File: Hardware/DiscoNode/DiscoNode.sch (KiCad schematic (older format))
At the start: 68 parts, among them J1 1267, J2 RJ45, J3 RJ45, J4 AVR-ISP-6, J5 Debug, J6 0026605020, Q1 NTR4003N, Q2 NTR4003N, Q3 NTR4003N, U1 ATMEGA328P-AU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

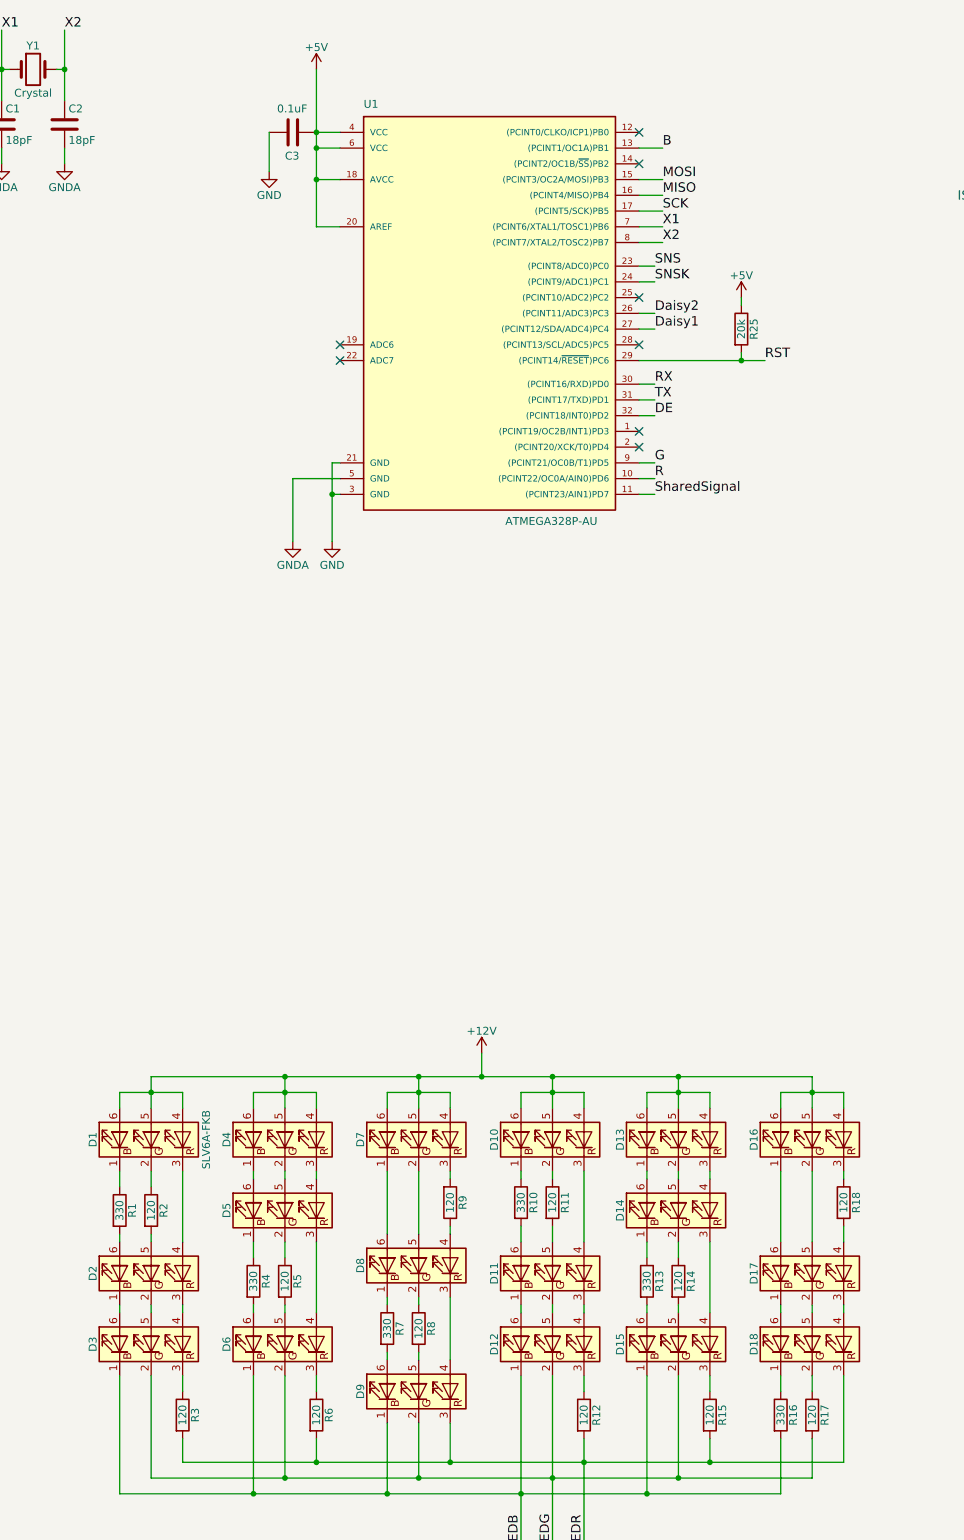
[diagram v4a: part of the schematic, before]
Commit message: Move debug pins.
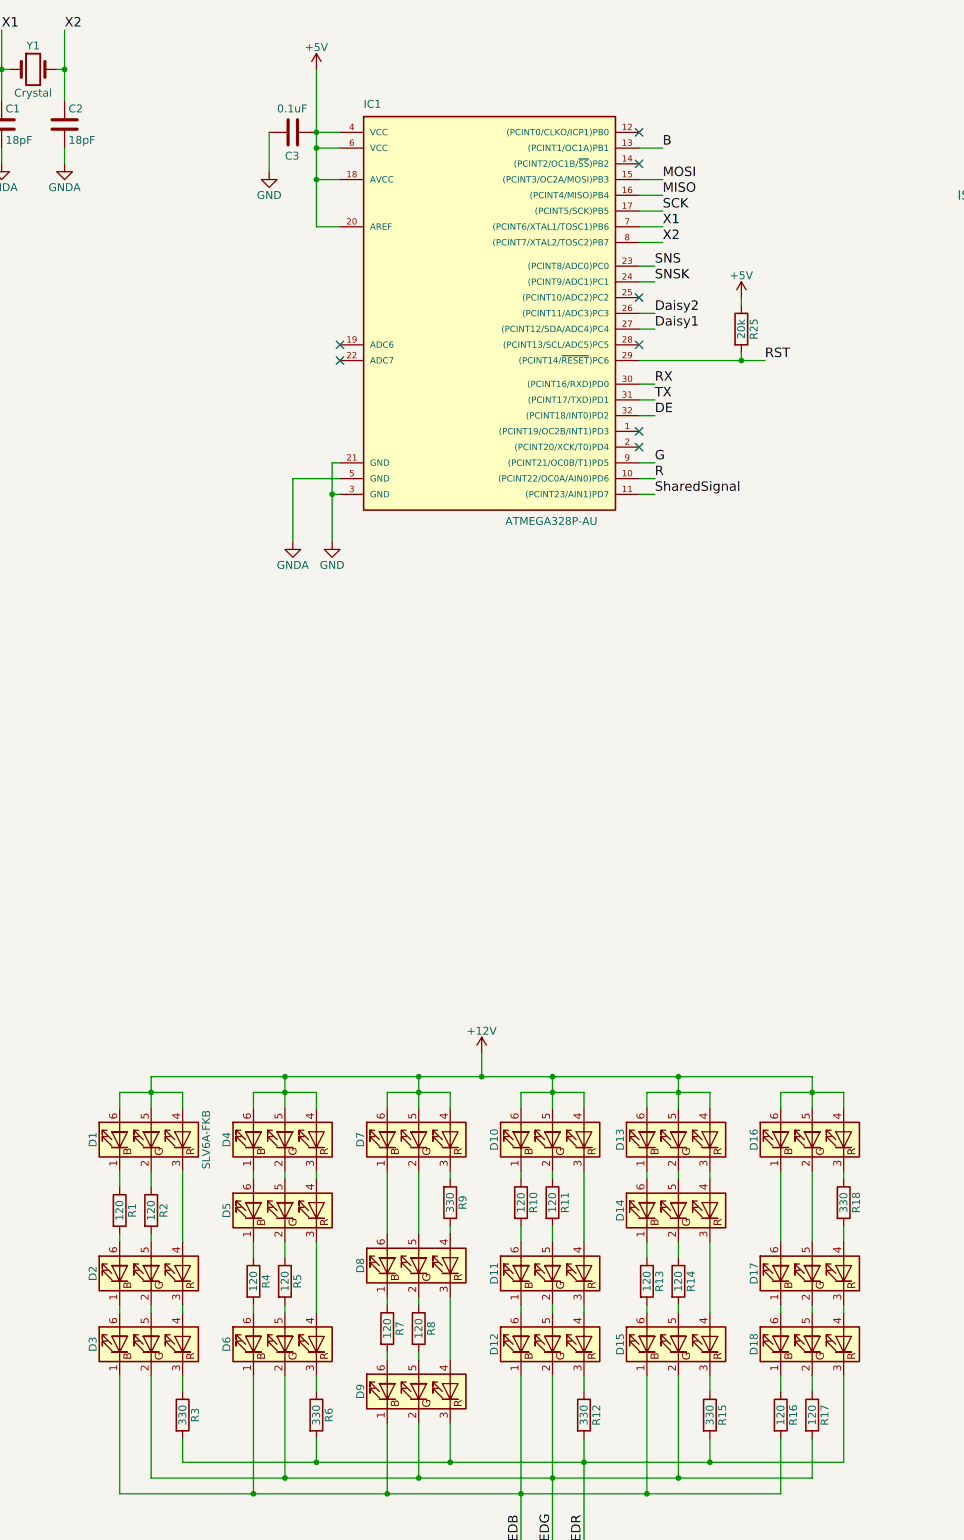
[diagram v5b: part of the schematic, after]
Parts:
- R1, R10, R13, R16, R4, R7: value 330 -> 120; Digikey RMCF0805JT330RCT-ND -> (none); MPN RMCF0805JT330R -> RMCF0805JT120R
- R12, R15, R18, R3, R6, R9: value 120 -> 330; Digikey RMCF0805JT120RCT-ND -> (none); MPN RMCF0805JT120R -> RMCF0805JT330R
- R2: Digikey RMCF0805JT120RCT-ND -> (none)
- renumbered U1 to IC1
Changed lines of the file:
@@
 P 1750 8450
 F 0 "R1" V 1830 8450 50  0000 C CNN
-F 1 "330" V 1750 8450 50  0000 C CNN
+F 1 "120" V 1750 8450 50  0000 C CNN
 F 2 "Resistors_SMD:R_0805" V 1680 8450 50  0001 C CNN
 F 3 "" H 1750 8450 50  0000 C CNN
-F 4 "RMCF0805JT330R" H 1750 8450 60  0001 C CNN "MPN"
-F 5 "RMCF0805JT330RCT-ND" H 1750 8450 60  0001 C CNN "Digikey"
+F 4 "RMCF0805JT120R" H 1750 8450 60  0001 C CNN "MPN"
 	1    1750 8450
 	1    0    0    -1
@@
 F 3 "" H 1950 8450 50  0000 C CNN
 F 4 "RMCF0805JT120R" H 1950 8450 60  0001 C CNN "MPN"
-F 5 "RMCF0805JT120RCT-ND" H 1950 8450 60  0001 C CNN "Digikey"
 	1    1950 8450
 	1    0    0    -1
@@
 P 2150 9750
 F 0 "R3" V 2230 9750 50  0000 C CNN
-F 1 "120" V 2150 9750 50  0000 C CNN
+F 1 "330" V 2150 9750 50  0000 C CNN
 F 2 "Resistors_SMD:R_0805" V 2080 9750 50  0001 C CNN
 F 3 "" H 2150 9750 50  0000 C CNN
-F 4 "RMCF0805JT120R" H 2150 9750 60  0001 C CNN "MPN"
-F 5 "RMCF0805JT120RCT-ND" H 2150 9750 60  0001 C CNN "Digikey"
+F 4 "RMCF0805JT330R" H 2150 9750 60  0001 C CNN "MPN"
 	1    2150 9750
 	1    0    0    -1
@@
 P 2600 8900
 F 0 "R4" V 2680 8900 50  0000 C CNN
-F 1 "330" V 2600 8900 50  0000 C CNN
+F 1 "120" V 2600 8900 50  0000 C CNN
 F 2 "Resistors_SMD:R_0805" V 2530 8900 50  0001 C CNN
 F 3 "" H 2600 8900 50  0000 C CNN
-F 4 "RMCF0805JT330R" H 2600 8900 60  0001 C CNN "MPN"
-F 5 "RMCF0805JT330RCT-ND" H 2600 8900 60  0001 C CNN "Digikey"
+F 4 "RMCF0805JT120R" H 2600 8900 60  0001 C CNN "MPN"
 	1    2600 8900
 	1    0    0    -1
@@
 P 3000 9750
 F 0 "R6" V 3080 9750 50  0000 C CNN
-F 1 "120" V 3000 9750 50  0000 C CNN
+F 1 "330" V 3000 9750 50  0000 C CNN
 F 2 "Resistors_SMD:R_0805" V 2930 9750 50  0001 C CNN
 F 3 "" H 3000 9750 50  0000 C CNN
-F 4 "RMCF0805JT120R" H 3000 9750 60  0001 C CNN "MPN"
-F 5 "RMCF0805JT120RCT-ND" H 3000 9750 60  0001 C CNN "Digikey"
+F 4 "RMCF0805JT330R" H 3000 9750 60  0001 C CNN "MPN"
 	1    3000 9750
 	1    0    0    -1
@@
 P 3450 9200
 F 0 "R7" V 3530 9200 50  0000 C CNN
-F 1 "330" V 3450 9200 50  0000 C CNN
+F 1 "120" V 3450 9200 50  0000 C CNN
 F 2 "Resistors_SMD:R_0805" V 3380 9200 50  0001 C CNN
 F 3 "" H 3450 9200 50  0000 C CNN
-F 4 "RMCF0805JT330R" H 3450 9200 60  0001 C CNN "MPN"
-F 5 "RMCF0805JT330RCT-ND" H 3450 9200 60  0001 C CNN "Digikey"
+F 4 "RMCF0805JT120R" H 3450 9200 60  0001 C CNN "MPN"
 	1    3450 9200
 	1    0    0    -1
@@
 P 3850 8400
 F 0 "R9" V 3930 8400 50  0000 C CNN
-F 1 "120" V 3850 8400 50  0000 C CNN
+F 1 "330" V 3850 8400 50  0000 C CNN
 F 2 "Resistors_SMD:R_0805" V 3780 8400 50  0001 C CNN
 F 3 "" H 3850 8400 50  0000 C CNN
-F 4 "RMCF0805JT120R" H 3850 8400 60  0001 C CNN "MPN"
-F 5 "RMCF0805JT120RCT-ND" H 3850 8400 60  0001 C CNN "Digikey"
+F 4 "RMCF0805JT330R" H 3850 8400 60  0001 C CNN "MPN"
 	1    3850 8400
 	1    0    0    1
@@
 P 4300 8400
 F 0 "R10" V 4380 8400 50  0000 C CNN
-F 1 "330" V 4300 8400 50  0000 C CNN
+F 1 "120" V 4300 8400 50  0000 C CNN
 F 2 "Resistors_SMD:R_0805" V 4230 8400 50  0001 C CNN
 F 3 "" H 4300 8400 50  0000 C CNN
-F 4 "RMCF0805JT330R" H 4300 8400 60  0001 C CNN "MPN"
-F 5 "RMCF0805JT330RCT-ND" H 4300 8400 60  0001 C CNN "Digikey"
+F 4 "RMCF0805JT120R" H 4300 8400 60  0001 C CNN "MPN"
 	1    4300 8400
 	1    0    0    -1
@@
 P 4700 9750
 F 0 "R12" V 4780 9750 50  0000 C CNN
-F 1 "120" V 4700 9750 50  0000 C CNN
+F 1 "330" V 4700 9750 50  0000 C CNN
 F 2 "Resistors_SMD:R_0805" V 4630 9750 50  0001 C CNN
 F 3 "" H 4700 9750 50  0000 C CNN
-F 4 "RMCF0805JT120R" H 4700 9750 60  0001 C CNN "MPN"
-F 5 "RMCF0805JT120RCT-ND" H 4700 9750 60  0001 C CNN "Digikey"
+F 4 "RMCF0805JT330R" H 4700 9750 60  0001 C CNN "MPN"
 	1    4700 9750
 	1    0    0    -1
@@
 P 5100 8900
 F 0 "R13" V 5180 8900 50  0000 C CNN
-F 1 "330" V 5100 8900 50  0000 C CNN
+F 1 "120" V 5100 8900 50  0000 C CNN
 F 2 "Resistors_SMD:R_0805" V 5030 8900 50  0001 C CNN
 F 3 "" H 5100 8900 50  0000 C CNN
-F 4 "RMCF0805JT330R" H 5100 8900 60  0001 C CNN "MPN"
-F 5 "RMCF0805JT330RCT-ND" H 5100 8900 60  0001 C CNN "Digikey"
+F 4 "RMCF0805JT120R" H 5100 8900 60  0001 C CNN "MPN"
 	1    5100 8900
 	1    0    0    -1
@@
 P 5500 9750
 F 0 "R15" V 5580 9750 50  0000 C CNN
-F 1 "120" V 5500 9750 50  0000 C CNN
+F 1 "330" V 5500 9750 50  0000 C CNN
 F 2 "Resistors_SMD:R_0805" V 5430 9750 50  0001 C CNN
 F 3 "" H 5500 9750 50  0000 C CNN
-F 4 "RMCF0805JT120R" H 5500 9750 60  0001 C CNN "MPN"
-F 5 "RMCF0805JT120RCT-ND" H 5500 9750 60  0001 C CNN "Digikey"
+F 4 "RMCF0805JT330R" H 5500 9750 60  0001 C CNN "MPN"
 	1    5500 9750
 	1    0    0    -1
@@
 P 5950 9750
 F 0 "R16" V 6030 9750 50  0000 C CNN
-F 1 "330" V 5950 9750 50  0000 C CNN
+F 1 "120" V 5950 9750 50  0000 C CNN
 F 2 "Resistors_SMD:R_0805" V 5880 9750 50  0001 C CNN
 F 3 "" H 5950 9750 50  0000 C CNN
-F 4 "RMCF0805JT330R" H 5950 9750 60  0001 C CNN "MPN"
-F 5 "RMCF0805JT330RCT-ND" H 5950 9750 60  0001 C CNN "Digikey"
+F 4 "RMCF0805JT120R" H 5950 9750 60  0001 C CNN "MPN"
 	1    5950 9750
 	1    0    0    -1
@@
 P 6350 8400
 F 0 "R18" V 6430 8400 50  0000 C CNN
-F 1 "120" V 6350 8400 50  0000 C CNN
+F 1 "330" V 6350 8400 50  0000 C CNN
 F 2 "Resistors_SMD:R_0805" V 6280 8400 50  0001 C CNN
 F 3 "" H 6350 8400 50  0000 C CNN
-F 4 "RMCF0805JT120R" H 6350 8400 60  0001 C CNN "MPN"
-F 5 "RMCF0805JT120RCT-ND" H 6350 8400 60  0001 C CNN "Digikey"
+F 4 "RMCF0805JT330R" H 6350 8400 60  0001 C CNN "MPN"
 	1    6350 8400
 	1    0    0    -1
@@
 $EndComp
 $Comp
-L ATMEGA328P-AU U1
+L ATMEGA328P-AU IC1
 U 1 1 5919154E
 P 4050 2700
-F 0 "U1" H 3300 3950 50  0000 L BNN
+F 0 "IC1" H 3300 3950 50  0000 L BNN
 F 1 "ATMEGA328P-AU" H 4200 1300 50  0000 L BNN
 F 2 "TQFP32" H 4050 2700 50  0001 C CIN
